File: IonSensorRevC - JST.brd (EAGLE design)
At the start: 50.8 x 22.9 mm, 19 parts, among them U1 REF2033AIDDCT, U2 INA826AIDR, U3 INA826AIDR, U4 INA826AIDR, X1 B4B-PH-K-S

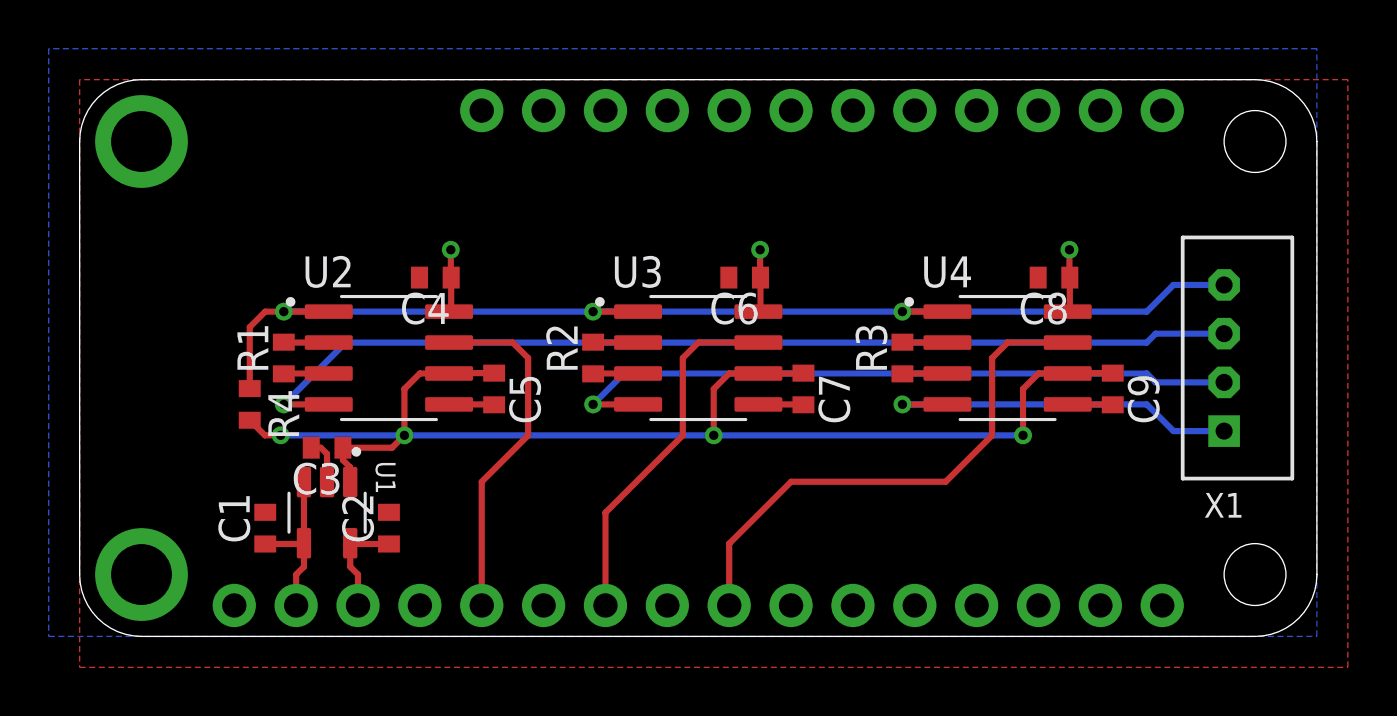
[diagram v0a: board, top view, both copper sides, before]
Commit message: Update traces
Updated traces to minimize noise
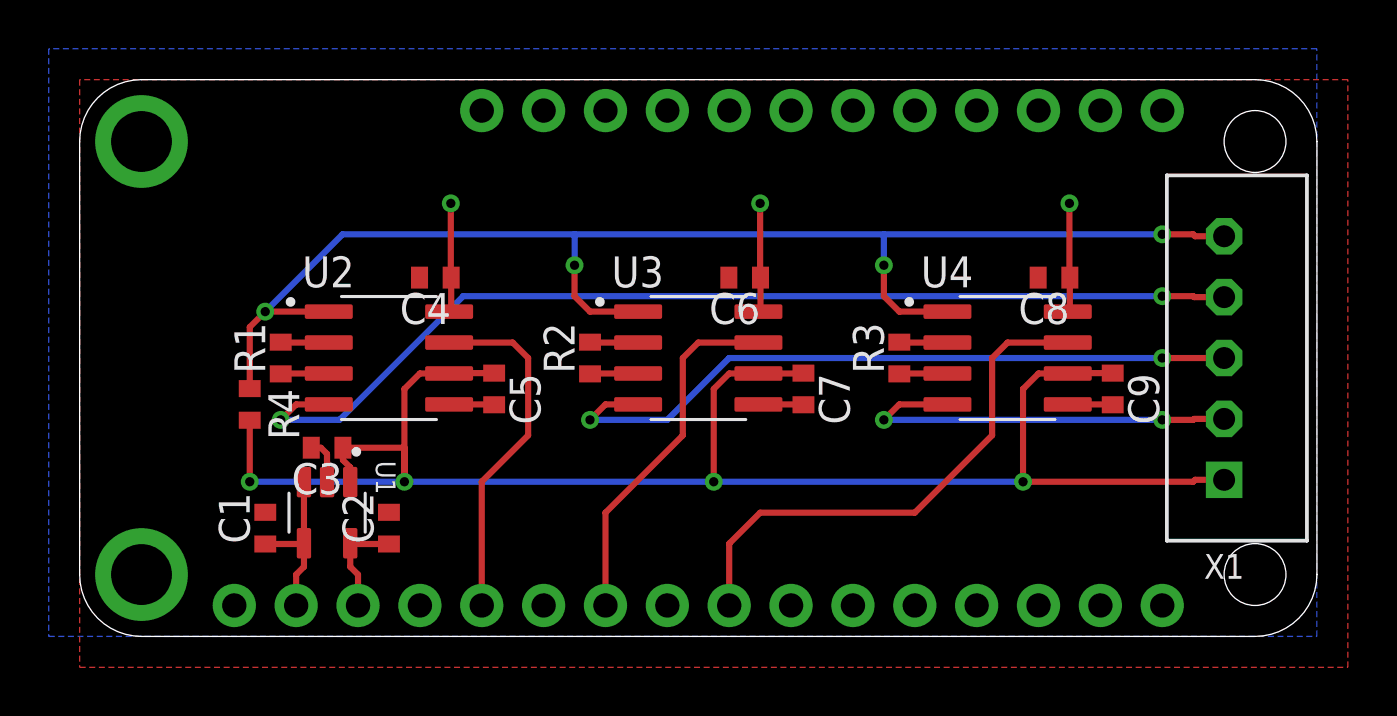
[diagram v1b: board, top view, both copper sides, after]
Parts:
- X1: value B4B-PH-K-S -> B5B-XH-2; device con-JST PH:B4B-PH-K-S -> con-JST XH:B5B-XH-A
- moved R2 0.13 mm to (21.0, 11.4)
- moved R1 0.13 mm to (8.26, 11.4)
- moved R3 0.13 mm to (33.7, 11.4)
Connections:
- removed net A1: MS1.6
- removed net A3: MS1.8
- removed net A5: MS1.10
- removed net CH1: U3.4, X1.2
- new net CH4: U4.4, X1.2
- net CH0: now also X1.4; no longer X1.3
- net CH2: now also U3.4, X1.3; no longer U4.4, X1.1
- net GND: now also MS1.10, MS1.6, MS1.8
- net REF: now also X1.5; no longer X1.4
- net VCC/2: now also X1.1
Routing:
- net CH1: track 28.4 -> 0.00 mm, vias 1 -> 0
- net VCC/2: track 53.9 -> 71.3 mm
- net CH4: track 0.00 -> 16.9 mm, vias 0 -> 2
- net CH2: track 15.5 -> 29.3 mm, vias 1 -> 2
- net REF: track 48.8 -> 57.6 mm, vias 3 -> 4
- net +3V3: track 14.5 -> 20.3 mm
- net CH0: track 41.7 -> 43.1 mm, vias 1 -> 2
